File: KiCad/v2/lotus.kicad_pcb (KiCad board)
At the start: 2 copper layers, 50 x 50 mm, 30 parts, among them J1 USB_B_Micro, J2 Conn_01x04, J3 Conn_01x02, SW1 SW_Push, SW2 SW_Push, U1 BQ24072, U2 ESP-12E, U3 MIC5504-3.3YM5, U4 Battery

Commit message: Organizado PCB
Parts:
- R6: moved to B.Cu
- moved R10 68.8 mm to (162.3, 117.3)
- moved C7 61.6 mm to (198.1, 112.3)
- moved R1 58.5 mm to (190.5, 111.8), turned to 90 degrees
- moved C3 54.6 mm to (185.7, 102.4), turned to 270 degrees
- moved R2 51.7 mm to (187.7, 104.6), turned to 180 degrees
- moved R11 48.8 mm to (162.3, 118.9)
- moved C1 48.7 mm to (200.9, 119.9), turned to 270 degrees
- moved R12 47.2 mm to (191.0, 105.7), turned to 180 degrees
- moved R8 44.5 mm to (191.1, 124.4), turned to 180 degrees
- moved U4 35.9 mm to (195.1, 104.0), turned to 45 degrees
- moved R13 35.8 mm to (193.8, 107.7), turned to 315 degrees
- moved C5 34.0 mm to (185.8, 123.9), turned to 180 degrees
- moved J2 32.7 mm to (186.6, 133.9), turned to 0 degrees
- moved C6 32.3 mm to (191.9, 115.8)
- moved R9 30.9 mm to (162.6, 112.5), turned to 90 degrees
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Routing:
- net VCC: track 0.00 -> 61.3 mm, vias 0 -> 5
- net COLOR_BUTTON: track 0.00 -> 42.8 mm, vias 0 -> 4
- net RST_BUTTON: track 0.00 -> 42.1 mm, vias 0 -> 2
- net TXD: track 0.00 -> 35.2 mm, vias 0 -> 2
- net PGOOD: track 0.00 -> 34.7 mm, vias 0 -> 2
- net RXD: track 0.00 -> 33.9 mm, vias 0 -> 2
- net GND: track 10.2 -> 43.9 mm, vias 1 -> 9
- net Net-(J3-Pad1): track 0.00 -> 33.1 mm, vias 0 -> 2
- net CHG: track 0.00 -> 31.7 mm, vias 0 -> 2
- net TS_BAT: track 0.00 -> 29.5 mm, vias 0 -> 2
- net OUT: track 0.50 -> 18.9 mm, vias 0 -> 3
- net BAT: track 0.00 -> 14.7 mm
- net LED_G: track 0.00 -> 11.7 mm
- net LED_B: track 0.00 -> 9.34 mm, vias 0 -> 2
- net LED_R: track 0.00 -> 6.62 mm
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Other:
- net class Default: clearance 0.1 -> 0.15; trace_width 0.25 -> 0.2
- net class Power: clearance 0.1 -> 0.15
- rule trace_clearance: 0.1 -> 0.15

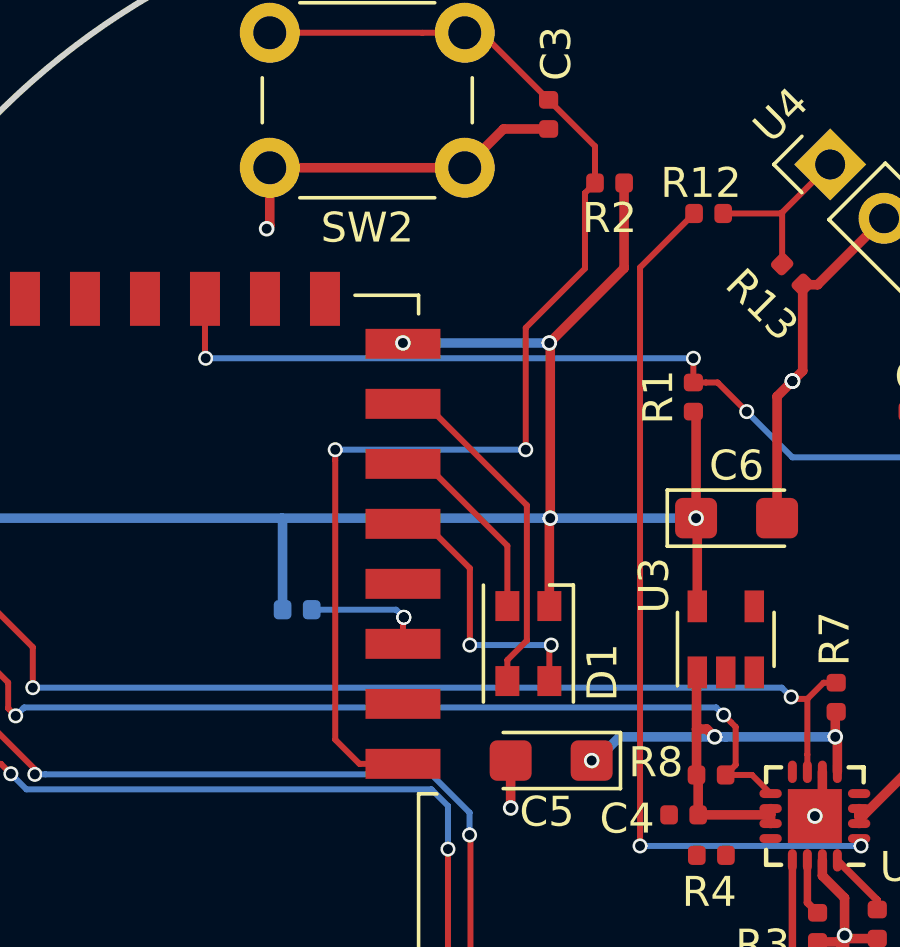
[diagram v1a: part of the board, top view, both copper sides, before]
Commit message: Adicionado resistores no led
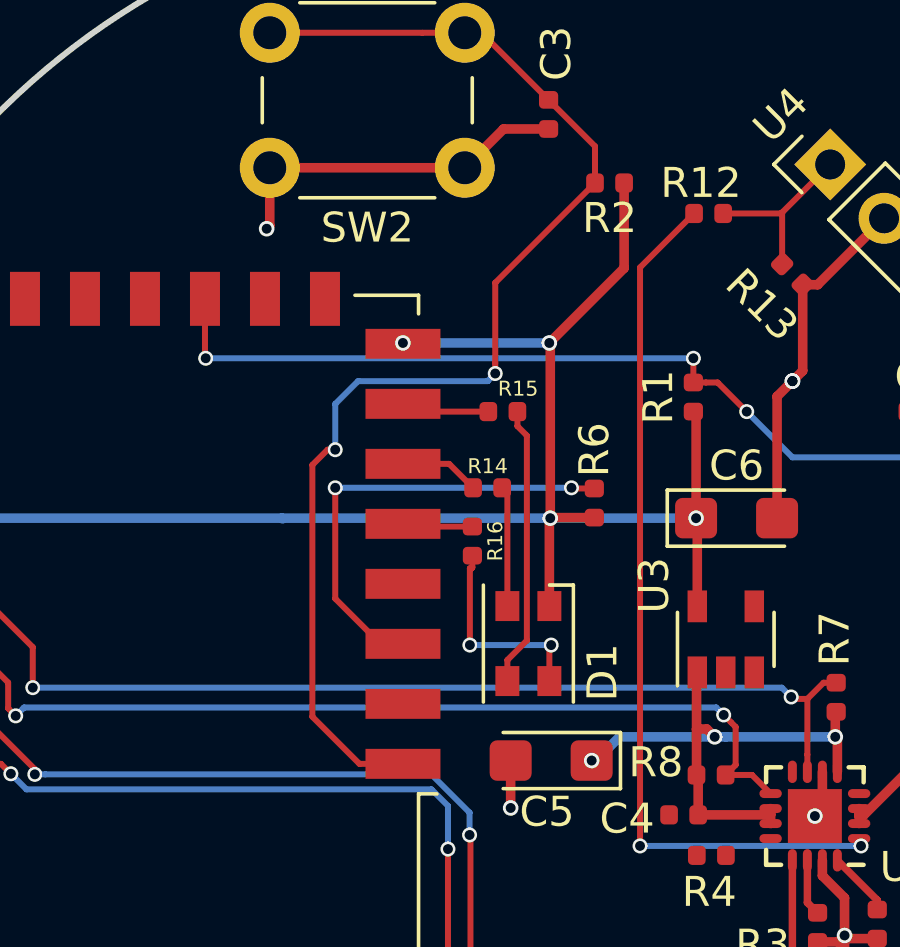
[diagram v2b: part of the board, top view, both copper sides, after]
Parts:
- added R14: 20, Resistor_SMD:R_0402_1005Metric, F.Cu at (183.6, 114.8)
- added R15: 10, Resistor_SMD:R_0402_1005Metric, F.Cu at (184.2, 112.3)
- added R16: 10, Resistor_SMD:R_0402_1005Metric, F.Cu at (183.1, 116.6)
- R6: moved to F.Cu
- moved R6 10.5 mm to (187.2, 115.3), turned to 90 degrees
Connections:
- D1 pad 2: LED_R -> Net-(D1-Pad2)
- D1 pad 3: LED_G -> Net-(D1-Pad3)
- D1 pad 4: LED_B -> Net-(D1-Pad4)
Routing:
- net Net-(R6-Pad2): track 4.07 -> 15.2 mm
- net Net-(D1-Pad3): track 0.00 -> 9.38 mm
- net Net-(D1-Pad4): track 0.00 -> 6.98 mm, vias 0 -> 2
- net LED_G: track 11.7 -> 4.74 mm
- net LED_B: track 9.34 -> 3.10 mm, vias 2 -> 0
- net Net-(D1-Pad2): track 0.00 -> 4.01 mm
- net LED_R: track 6.62 -> 4.17 mm
- net VCC: track 61.3 -> 59.8 mm
